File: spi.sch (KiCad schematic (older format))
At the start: 13 parts, among them U5 MS5611-01BA03, U6 MPU-6000, U7 MPU-9250

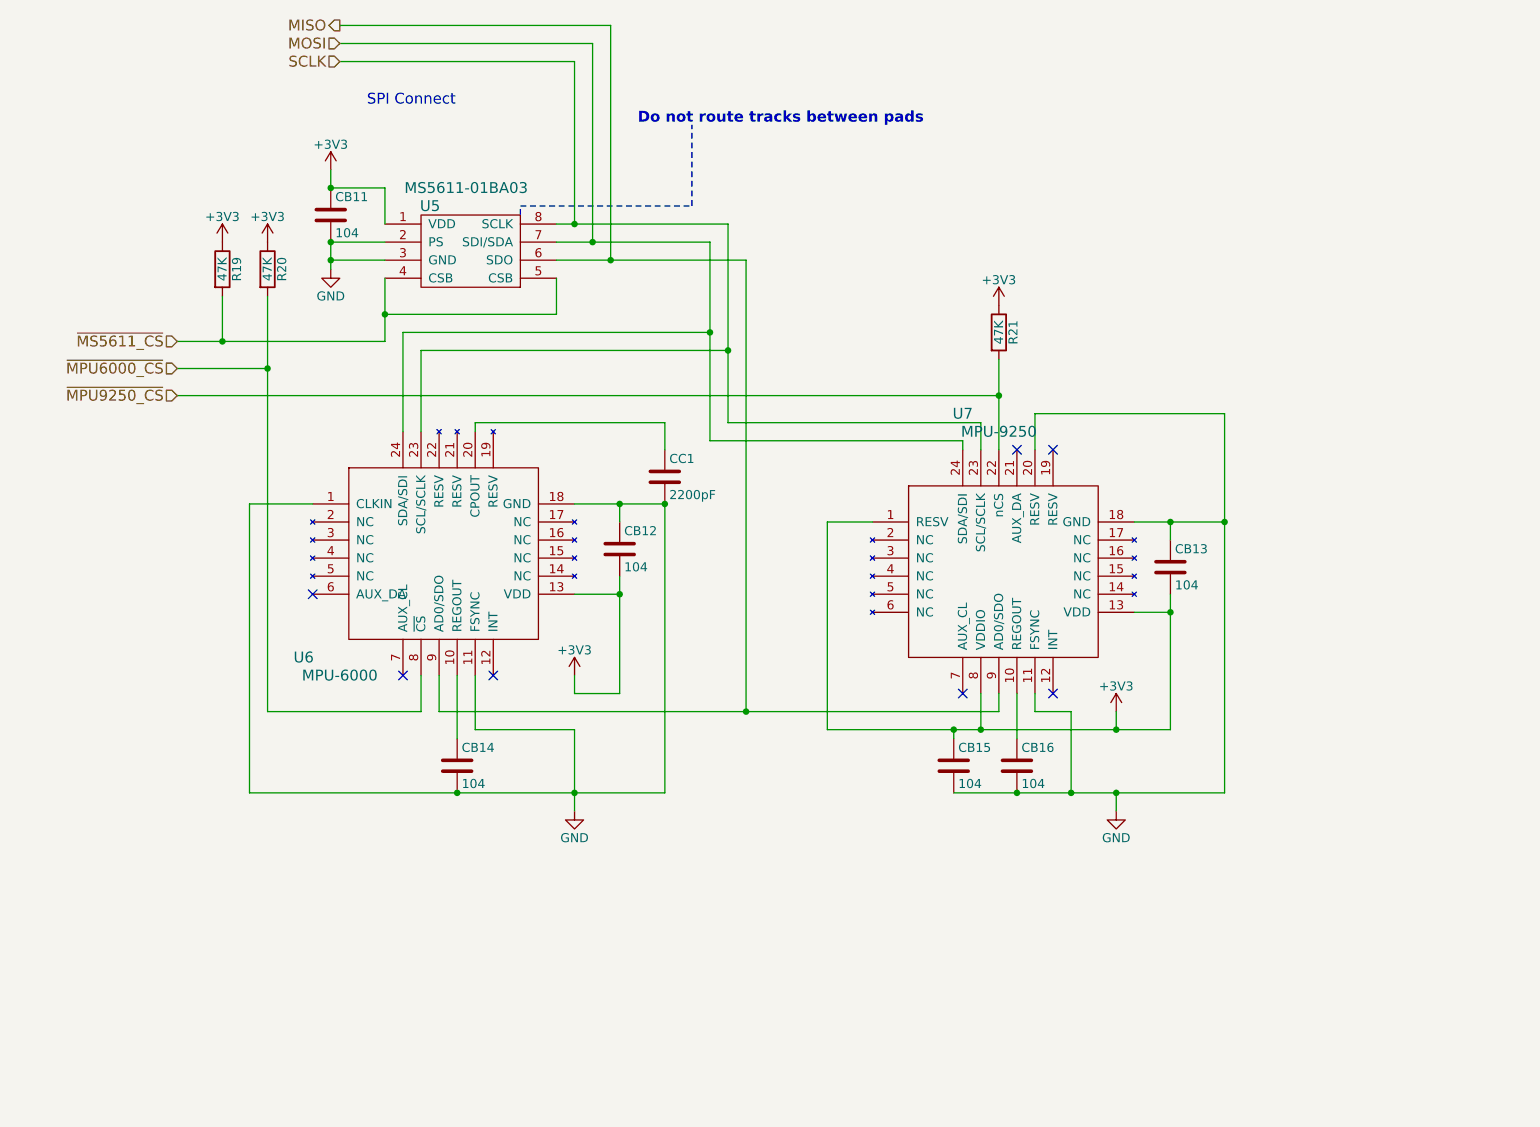
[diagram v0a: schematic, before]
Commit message: Improved the pin comatibility to match with other ardupilot project.
Signed-off-by: Akira Tsukamoto <akira-t@s9.dion.ne.jp>
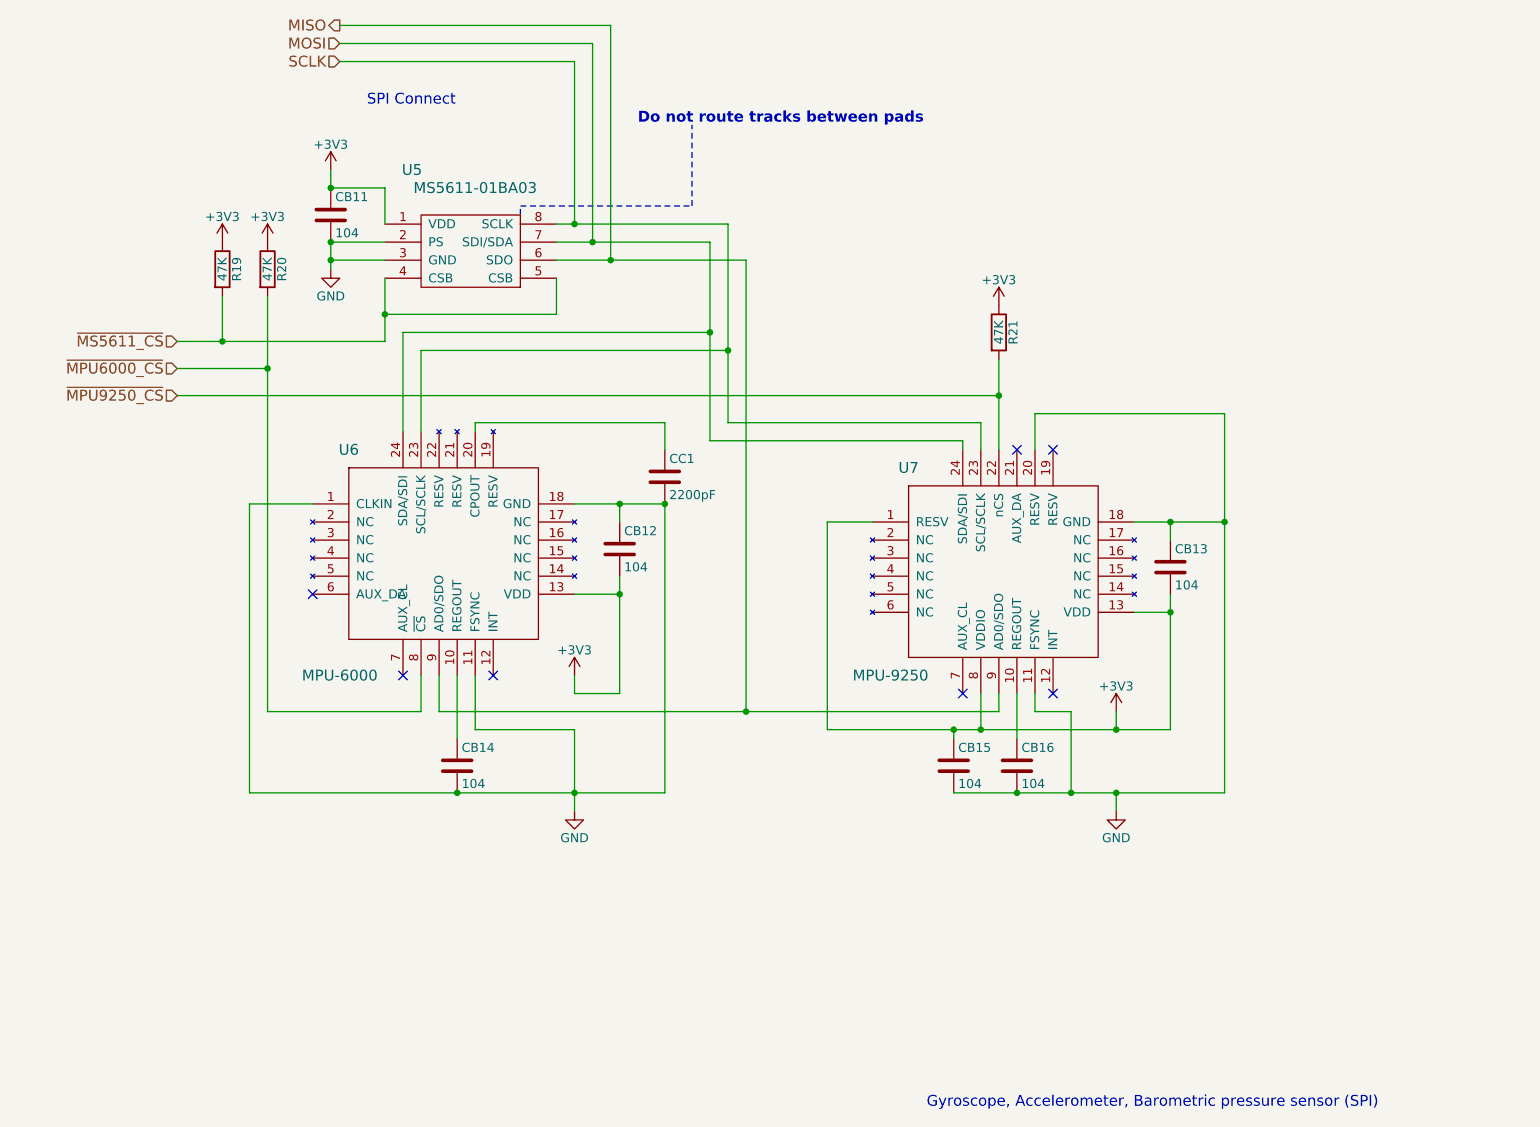
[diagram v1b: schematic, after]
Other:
- note added: "Gyroscope, Accelerometer, Barometric pressure sensor (SPI)"
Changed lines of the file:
@@
 U 1 1 56F6D3C2
 P 4650 3700
-F 0 "U6" H 3850 2400 60  0000 C CNN
+F 0 "U6" H 4100 3550 60  0000 C CNN
 F 1 "MPU-6000" H 4050 2300 60  0000 C CNN
 F 2 "droneworks:QFN-4-24_MPU-90X0_droneworks" H 4650 3700 60  0001 C CNN
@@
 U 1 1 56F6D3D0
 P 4750 2400
-F 0 "U5" H 4550 2300 60  0000 C CNN
-F 1 "MS5611-01BA03" H 4750 2400 60  0000 C CNN
+F 0 "U5" H 4450 2500 60  0000 C CNN
+F 1 "MS5611-01BA03" H 4800 2400 60  0000 C CNN
 F 2 "droneworks:MS5611-01BA03_droneworks" H 4750 2400 60  0001 C CNN
 F 3 "" H 4750 2400 60  0000 C CNN
@@
 U 1 1 58D13D21
 P 7750 3800
-F 0 "U7" H 7500 3950 60  0000 C CNN
-F 1 "MPU-9250" H 7700 3850 60  0000 C CNN
+F 0 "U7" H 7200 3650 60  0000 C CNN
+F 1 "MPU-9250" H 7100 2500 60  0000 C CNN
 F 2 "droneworks:QFN-3-24_MPU-9250_droneworks" H 7750 3800 60  0001 C CNN
 F 3 "" H 7750 3800 60  0000 C CNN
@@
 Text Notes 5700 2050 0    60   ~ 12
 Do not route tracks between pads
+Text Notes 7300 7500 0    60   ~ 0
+Gyroscope, Accelerometer, Barometric pressure sensor (SPI)
 $EndSCHEMATC
